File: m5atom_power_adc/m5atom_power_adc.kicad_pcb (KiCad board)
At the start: 2 copper layers, 80 x 78 mm, 145 parts, among them J101 USB_C_Receptacle_USB2.0_16P, J102 Conn_01x04_Pin, J103 SubBatt, J104 MainBatt, J105 I2C, J106 Shunt, J201 Relay0, J202 R0SW, J301 Relay1, J302 R1SW, J401 Relay2, J402 R2SW, J501 GROVE-CONNECTOR, J601 GROVE-CONNECTOR, Q101 AO3401A, Q102 MMBT2222A, Q103 AO3401A, Q201 MMBT2222A, Q301 MMBT2222A, Q401 MMBT2222A, Q501 AO3401A, Q502 MMBT2222A, Q601 AO3401A, Q602 MMBT2222A, SW101 Boot, SW102 Reset, SW103 Btn0, SW104 Btn1, U101 LM2596S-5, U102 AMS1117-3.3, U103 ESP32-S3-MINI-1, U104 AMS1117-3.3, U106 ADS1115IDGS, U108 INA228

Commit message: chore: Grove LED色変更・リレー抵抗を680Ω 500mWに変更・INA228品番更新
Co-Authored-By: Claude Sonnet 4.6 <noreply@anthropic.com>
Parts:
- removed R204, R304, R404: 1k, Resistor_SMD:R_0603_1608Metric
- R104: value 1k -> 200
- R203, R303, R403: value 1k -> 680 500mW; footprint Resistor_SMD:R_0603_1608Metric -> Resistor_SMD:R_0805_2012Metric
- moved R203 2.43 mm to (96.6, 65.9), turned to 0 degrees
- moved R403 2.42 mm to (96.6, 90.9), turned to 0 degrees
- moved R303 2.41 mm to (96.6, 78.4), turned to 0 degrees
- moved TP101 0.89 mm to (94.9, 75.7)
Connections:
- R203 pad 2: Net-(R203-Pad2) -> Net-(D202-A)
- R303 pad 2: Net-(R303-Pad2) -> Net-(D302-A)
- R403 pad 2: Net-(R403-Pad2) -> Net-(D402-A)
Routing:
- net +12V: track 97.0 -> 99.8 mm
- net Net-(R403-Pad2): track 2.05 -> 0.00 mm
- net Net-(R303-Pad2): track 2.05 -> 0.00 mm
- net Net-(R203-Pad2): track 2.05 -> 0.00 mm
- net GNDA: vias 18 -> 21
- net GND2: vias 27 -> 29
- net GND1: vias 37 -> 42

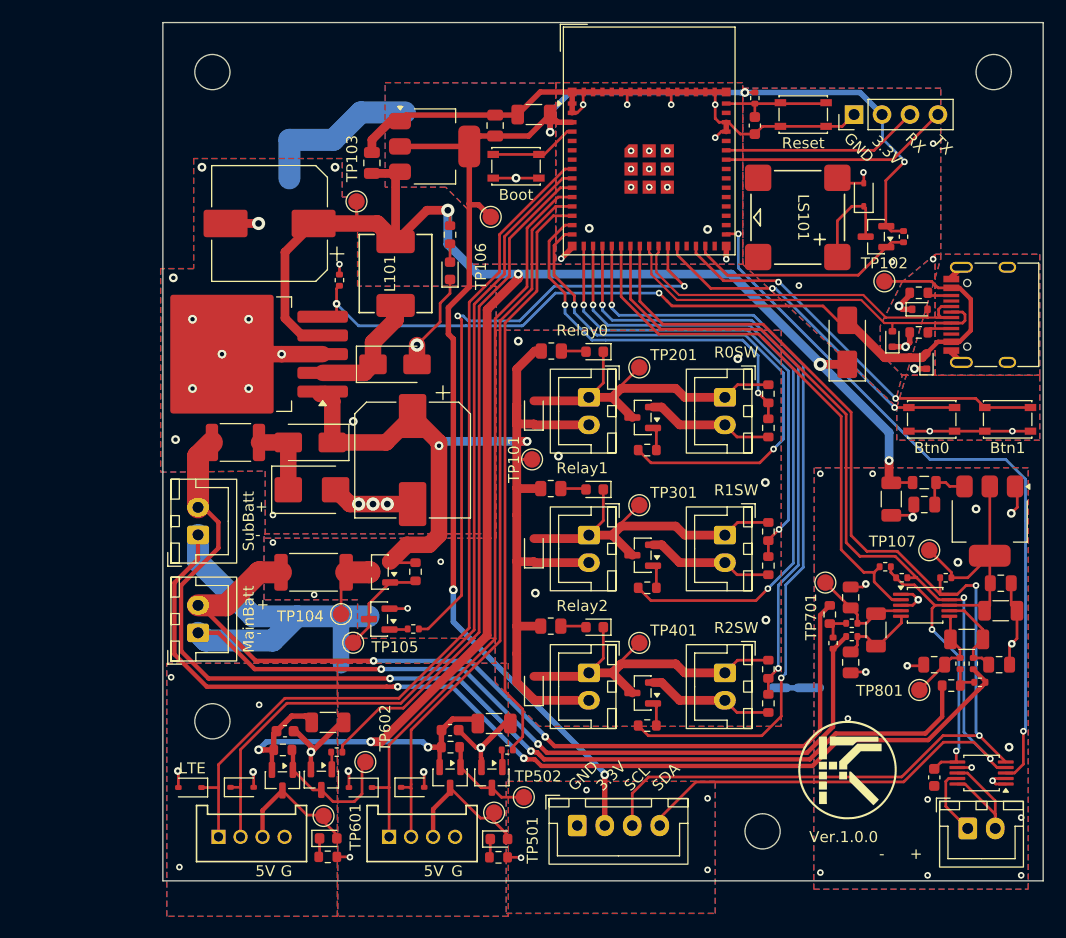
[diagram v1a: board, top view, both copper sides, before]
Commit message: feat: m5atom_power_adc 回路・PCB を更新
KiCad 上で行った回路設計・PCB レイアウト変更を反映。
変更内容の詳細は KiCad 上で差分を確認すること。

Co-Authored-By: Claude Sonnet 4.6 <noreply@anthropic.com>
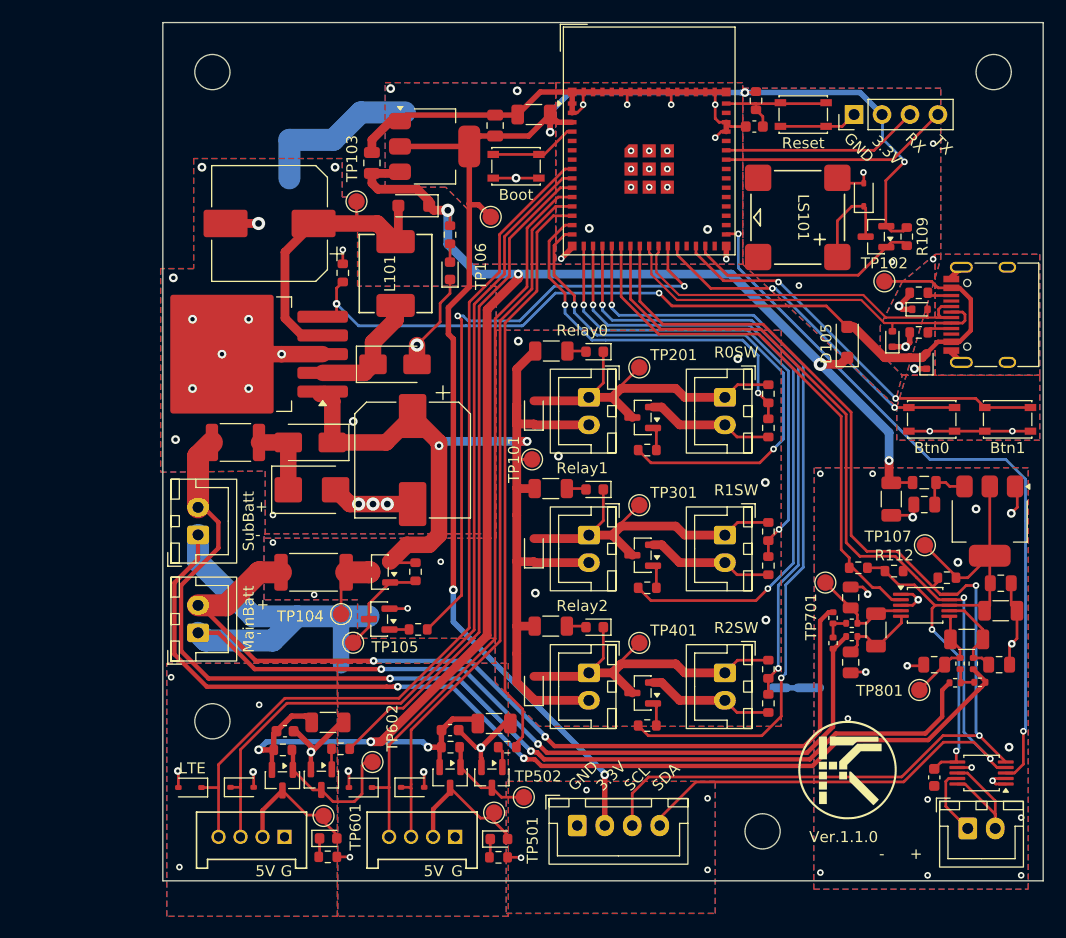
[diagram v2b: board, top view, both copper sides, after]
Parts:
- added D110: 2A, Diode_SMD:D_SOD-123F, F.Cu at (84.1, 52.7)
- D105: value SSL36 -> 2A; footprint Diode_SMD:D_SMA -> Diode_SMD:D_SOD-123F
- R101: value 10k -> 100k; footprint Resistor_SMD:R_0402_1005Metric -> Resistor_SMD:R_0603_1608Metric
- R104, R501, R601: value 200 -> 390
- R105, R108, R109, R111, R112, R113, R503, R603: footprint Resistor_SMD:R_0402_1005Metric -> Resistor_SMD:R_0603_1608Metric
- R203, R303, R403: value 680 500mW -> 1.5k; footprint Resistor_SMD:R_0805_2012Metric -> Resistor_SMD:R_1206_3216Metric
- R701, R801: footprint Resistor_SMD:R_0603_1608Metric -> Resistor_SMD:R_0402_1005Metric
- moved R111 2.45 mm to (124.5, 85.6)
- moved R112 0.92 mm to (127.8, 85.9)
- moved R101 0.73 mm to (77.7, 58.8)
- moved TP602 0.65 mm to (80.4, 103.2)
- moved TP107 0.60 mm to (130.6, 83.5)
- moved R603 0.46 mm to (77.5, 102.0)
- moved R108 0.44 mm to (84.5, 91.2)
- moved R801 0.44 mm to (133.3, 96.0)
- moved R701 0.43 mm to (122.2, 90.1)
- moved R109 0.29 mm to (128.9, 55.5)
- moved R105 0.26 mm to (115.2, 43.1)
- moved R503 0.25 mm to (92.6, 101.9)
- moved R113 0.11 mm to (132.6, 86.5)
- moved C104 0.10 mm to (115.1, 45.5), turned to 180 degrees
- turned J501 to 0 degrees
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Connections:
- C102 pad 1: +5V -> Net-(D110-A)
- J501 pad 1: /GU_0 -> GND1
- J501 pad 2: /GU_1 -> Net-(D501-A)
- J501 pad 3: Net-(D501-A) -> /GU_1
- J501 pad 4: GND1 -> /GU_0
- J601 pad 1: /LTE_RX -> GND1
- J601 pad 2: /LTE_TX -> Net-(D601-A)
- J601 pad 3: Net-(D601-A) -> /LTE_TX
- J601 pad 4: GND1 -> /LTE_RX
- L101 pad 2: +5V -> Net-(D110-A)
- R104 pad 1: +5V -> Net-(D108-A)
- R104 pad 2: Net-(D108-A) -> +5V
- TP103 pad 1: +5V -> Net-(D110-A)
- U101 pad 4: +5V -> Net-(D110-A)
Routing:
- net Net-(D110-A): track 0.00 -> 27.4 mm
- net +5V: track 181.5 -> 154.3 mm
- net GND2: track 100.9 -> 96.6 mm, vias 29 -> 31
- net +3.3VA: track 47.5 -> 49.7 mm
- net EN: track 10.3 -> 11.5 mm
- net /LTE_EN: track 61.8 -> 60.7 mm
- net /SDA: track 105.9 -> 105.0 mm
- net /CHG_ON: track 57.0 -> 56.3 mm
- net /ADC_READY: track 50.6 -> 49.9 mm
- net +BATT: track 99.7 -> 100.3 mm
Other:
- board text added: "Ver.1.1.0"
- board text removed: "Ver.1.0.0"

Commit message: feat: 緊急充電回路をバイポーラトランジスタ構成に変更
P-ch MOSFET（AO3401A）をPNPトランジスタに置き換え、ボディダイオードによる
逆電流を防止。ベース電流制限抵抗（R114 470Ω）を追加しQ102の過熱を防ぐ。

Co-Authored-By: Claude Sonnet 4.6 <noreply@anthropic.com>
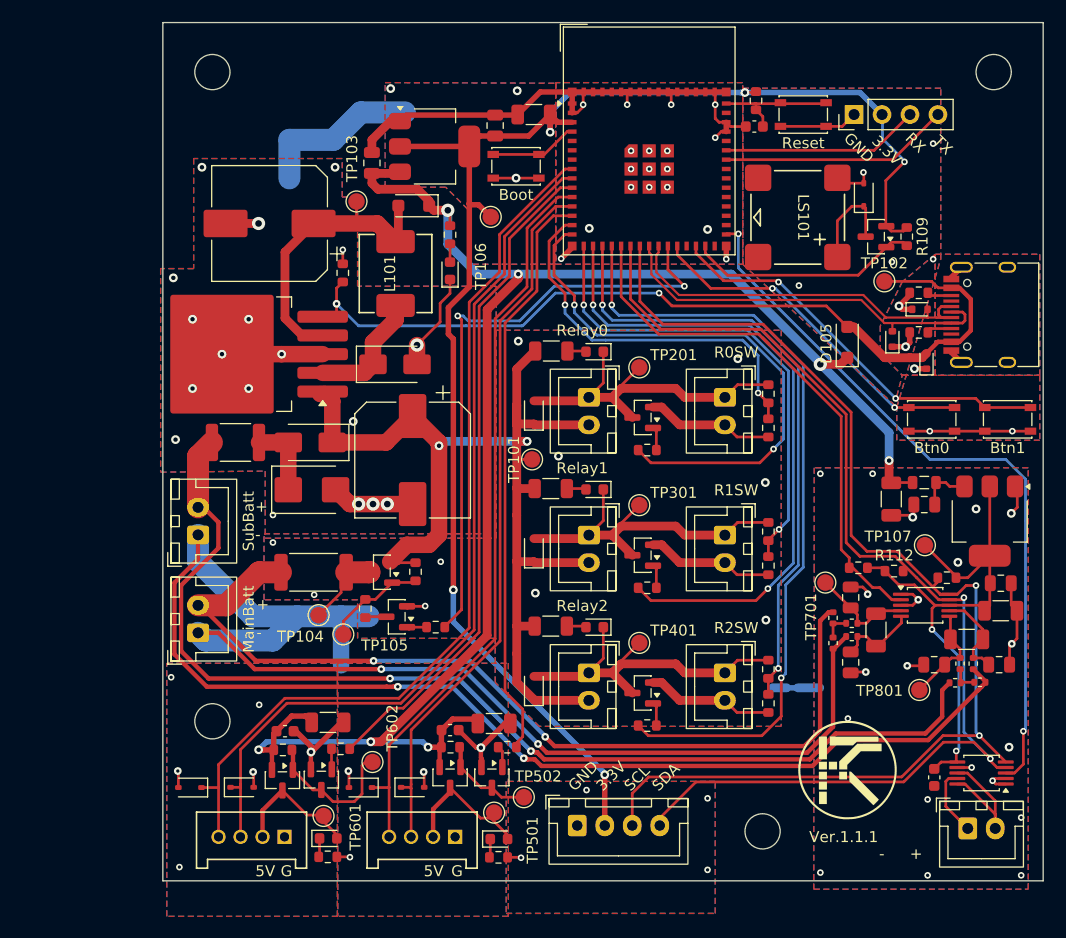
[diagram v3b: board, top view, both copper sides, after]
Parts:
- removed Q101: AO3401A, Package_TO_SOT_SMD:SOT-23
- added Q104: Q_PNP_BEC, Package_TO_SOT_SMD:SOT-23, F.Cu at (81.2, 86.0)
- added R114: 470, Resistor_SMD:R_0603_1608Metric, F.Cu at (79.7, 89.3)
- R101: value 100k -> 1k
- moved TP104 2.05 mm to (75.5, 89.9)
- moved Q102 1.61 mm to (82.6, 90.0)
- moved R108 1.61 mm to (86.1, 91.0)
- moved TP105 1.17 mm to (77.7, 91.6)
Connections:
- Q102 pad 3: Net-(Q101-G) -> Net-(Q102-C)
- R106 pad 2: Net-(Q101-G) -> Net-(Q104-B)
- TP105 pad 1: Net-(Q101-G) -> Net-(Q104-B)
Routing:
- net Net-(Q104-B): track 0.00 -> 9.43 mm
- net Net-(Q101-G): track 9.23 -> 0.00 mm
- net Net-(Q102-C): track 0.00 -> 1.94 mm
- net Net-(Q104-C): track 6.13 -> 7.06 mm
- net /CHG_ON: track 56.3 -> 55.4 mm
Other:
- board text added: "Ver.1.1.1"
- board text removed: "LTE"
- board text removed: "Ver.1.1.0"

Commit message: feat(m5atom_power_adc): 逆極性保護を理想ダイオード(LM73100)に置き換え、電源スイッチ＆自己保持回路を追加（作業途中）
- LM73100用カスタム記号・フットプリント(VQFN-10-HR)を追加
- 電源回路をサブシートに分離(power.kicad_sch)
- PCBレイアウト更新

Co-Authored-By: Claude Sonnet 4.6 <noreply@anthropic.com>
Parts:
- removed the D101 at (74.8, 78.5)
- removed the D102 at (74.7, 74.2)
- removed F101: Polyfuse, Fuse:Fuse_1812_4532Metric
- removed the TP101 at (94.9, 75.7)
- added C901: 1uF X7R, Capacitor_SMD:C_0603_1608Metric, F.Cu at (75.3, 79.3)
- added C902: 1uF X7R, Capacitor_SMD:C_0603_1608Metric, F.Cu at (77.5, 79.4)
- added C903: 470pF, Capacitor_SMD:C_0603_1608Metric, F.Cu at (76.8, 73.1)
- added C904: 47uF, Capacitor_SMD:C_1206_3216Metric, F.Cu at (57.0, 74.2)
- added D901: SMAJ16A, Diode_SMD:D_SMB, F.Cu at (72.1, 75.8)
- added F901: Polyfuse, Fuse:Fuse_1812_4532Metric, F.Cu at (66.6, 74.1)
- added Q901: Q_PMOS_GSD, Package_TO_SOT_SMD:SOT-23, F.Cu at (51.8, 70.0)
- added Q902: MMBT2222A, Package_TO_SOT_SMD:SOT-23, F.Cu at (51.8, 74.5)
- added R901: 390k, Resistor_SMD:R_0603_1608Metric, F.Cu at (73.8, 82.5)
- added R902: 56k, Resistor_SMD:R_0603_1608Metric, F.Cu at (76.8, 82.5)
- added R903: 10k, Resistor_SMD:R_0603_1608Metric, F.Cu at (56.2, 77.2)
- added R904: 100k, Resistor_SMD:R_0603_1608Metric, F.Cu at (56.2, 79.7)
- added R905: 100, Resistor_SMD:R_0402_1005Metric, F.Cu at (50.8, 77.7)
- added SW901: Boot, Button_Switch_SMD:SW_SPST_PTS810, F.Cu at (57.6, 70.2)
- added U901: ~, 000_Local:VQFN-10-HR(2x2), F.Cu at (76.4, 75.5)
- renumbered C110 to C111, D103 to D101, D104 to D102, D105 to D103, D106 to D104, D107 to D105, D110 to D106, D108 to D107, D109 to D108, Q104 to Q101, R114 to R108, R108 to R109, R109 to R110, R111 to R112, R112 to R113, R113 to R114, R205 to R204, R305 to R304, R405 to R404, TP102 to TP101, TP103 to TP102, TP104 to TP103, TP105 to TP104, TP106 to TP105, TP107 to TP106, U108 to U107
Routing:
- net Net-(D901-A1): track 0.00 -> 22.7 mm
- net +12V: track 99.8 -> 110.6 mm
- net Net-(U901-EN/UVLO): track 0.00 -> 7.58 mm
- net Net-(D101-A1): track 6.96 -> 0.00 mm
- net GND1: track 103.2 -> 107.6 mm, vias 42 -> 43
- net Net-(U901-DVDT): track 0.00 -> 1.61 mm
- added copper zone on F.Cu, net +12V
- added copper zone on F.Cu, net Net-(D901-A1)

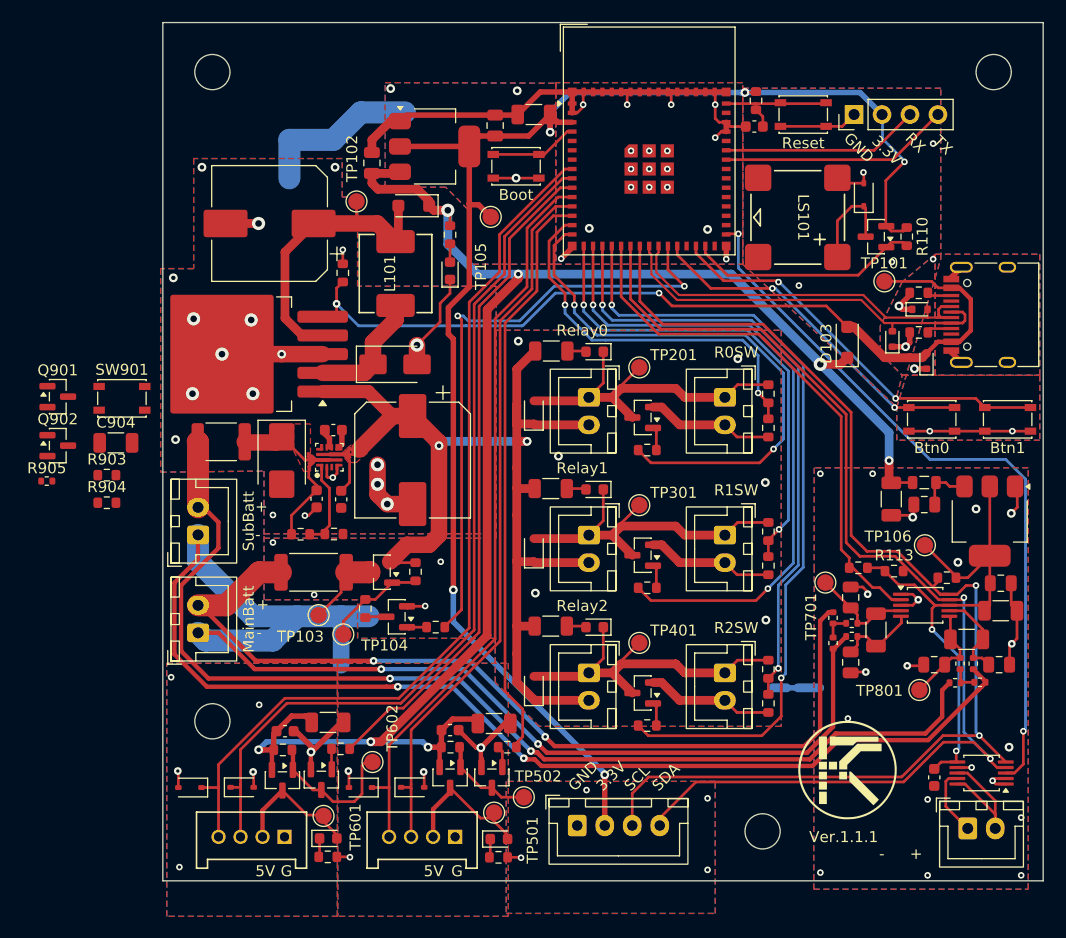
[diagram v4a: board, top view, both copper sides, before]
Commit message: feat(m5atom_power_adc): リレー状態検出をアナログ分圧からI2C入力に変更
- 分圧抵抗(R201/R202/R301/R302/R401/R402)とRelaySenseラベルを削除
- I2Cコネクタ(J107/J108)を追加、GP2/GP3/GP11/GP12・PWR_HOLDラベルを追加
- +12VAラベルを+12VRAWにリネーム
- ネットクラスの配線幅プリセットに1.0mmを追加
- PCBのネット再割当て・DRC警告を解消

Co-Authored-By: Claude Sonnet 5 <noreply@anthropic.com>
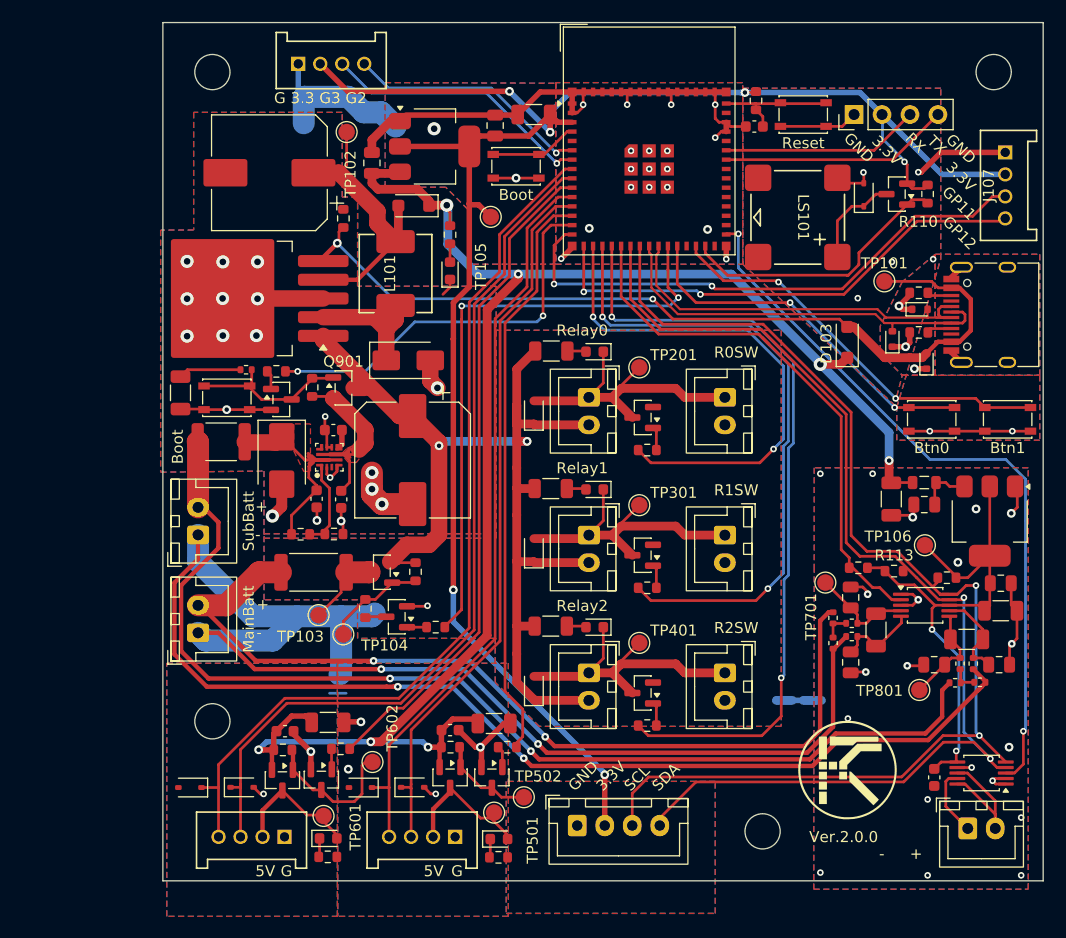
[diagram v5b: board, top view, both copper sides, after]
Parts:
- removed R201, R301, R401: 100k, Resistor_SMD:R_0603_1608Metric
- removed R202, R302, R402: 27k, Resistor_SMD:R_0603_1608Metric
- added J107: I2C, 000_Local:HY2.0-4PZZ, F.Cu at (137.9, 50.8)
- added J108: I2C, 000_Local:HY2.0-4PZZ, F.Cu at (76.6, 39.8)
- moved Q901 26.0 mm to (77.7, 69.2)
- moved R904 21.4 mm to (74.9, 69.2), turned to 90 degrees
- moved R905 20.7 mm to (68.9, 67.6), turned to 180 degrees
- moved Q902 20.7 mm to (72.1, 70.3)
- moved R903 18.1 mm to (71.6, 67.7), turned to 180 degrees
- moved SW901 9.53 mm to (67.1, 70.1)
- moved C904 7.43 mm to (62.9, 69.7), turned to -90 degrees
- moved TP102 6.37 mm to (78.0, 46.0)
- moved U101 5.06 mm to (68.2, 61.1)
- moved R101 4.95 mm to (77.7, 53.8)
- moved C102 4.61 mm to (71.0, 49.7)
- moved R110 4.31 mm to (130.8, 51.6)
- moved Q103 4.31 mm to (128.0, 51.6)
- moved NT102 4.14 mm to (76.2, 42.8)
- moved D105 1.26 mm to (83.6, 66.7)
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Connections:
- net /Power/+12VA renamed /Power/+12VRAW
- R903 pad 1: /Power/PWR_HOLD -> /PWR_HOLD
- U103 pad 14: /RelaySense0 -> /PWR_HOLD
- U103 pad 15: /Relay0 -> /GP11
- U103 pad 16: /RelaySense1 -> /GP12
- U103 pad 17: /Relay1 -> /Relay0
- U103 pad 18: /RelaySense2 -> /Relay1
- U103 pad 6: unconnected-(U103-IO2-Pad6) -> /GP2
- U103 pad 7: unconnected-(U103-IO3-Pad7) -> /GP3
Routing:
- net /RelaySense2: track 56.7 -> 0.00 mm, vias 2 -> 0
- net /GP11: track 0.00 -> 50.2 mm, vias 0 -> 2
- net /GP12: track 0.00 -> 45.5 mm, vias 0 -> 2
- net /RelaySense1: track 44.4 -> 0.00 mm, vias 2 -> 0
- net /PWR_HOLD: track 0.00 -> 36.0 mm, vias 0 -> 2
- net /RelaySense0: track 35.1 -> 0.00 mm, vias 2 -> 0
- net +3.3V: track 138.7 -> 170.8 mm, vias 5 -> 6
- net GND1: track 107.6 -> 75.6 mm, vias 43 -> 26
- net /GP3: track 0.00 -> 24.8 mm, vias 0 -> 1
- net /GP2: track 0.00 -> 22.3 mm, vias 0 -> 1
- net /Power/+12VRAW: track 0.00 -> 20.2 mm
- net Net-(Q901-G): track 0.00 -> 14.9 mm
- net +12V: track 110.6 -> 97.4 mm
- net GND2: track 96.6 -> 103.1 mm, vias 31 -> 30
- net Net-(C904-Pad1): track 0.00 -> 5.71 mm
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- added copper zone on F.Cu, net /Power/+12VRAW
- removed copper zone on F.Cu, net +12V
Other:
- board text added: "G 3.3 G3 G2"
- board text added: "GP11"
- board text added: "GP12"
- board text added: "Ver.2.0.0"
- board text removed: "Ver.1.1.1"
